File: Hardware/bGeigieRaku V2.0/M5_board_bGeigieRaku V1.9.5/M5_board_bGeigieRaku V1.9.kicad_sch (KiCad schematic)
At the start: 22 parts, among them J1 M5 2x15 pin, J10 QI GND, J11 QI charger Plus, J2 Geiger, J3 GPS, J4 Conn_01x14_Female, J5 Conn_01x14_Female, J6 Conn_01x14_Female, J7 Conn_01x14_Female, J8 QI charger GND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

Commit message: Updated board V1.9.6
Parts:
- removed J4, J5, J6: Conn_01x14_Female, Connector_PinHeader_2.54mm:PinHeader_1x18_P2.54mm_Vertical, symbol Connector:Conn_01x18_Female
- J1: footprint Connector_PinHeader_2.54mm:PinHeader_2x15_P2.54mm_Vertical -> Connector_PinHeader_2.54mm:PinHeader_2x15_P2.54mm_Vertical_SMD
- J3: footprint Connector_PinHeader_2.54mm:PinHeader_1x04_P2.54mm_Horizontal -> Connector_PinHeader_1.00mm:PinHeader_1x04_P1.00mm_Horizontal
- J7: symbol Connector:Conn_01x18_Female -> Connector:Conn_01x08_Male
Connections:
- net 3.3V: now also J2.1 (Pin_1); no longer J2.3 (Pin_3)
- net GND: now also J2.3 (Pin_3); no longer J2.1 (Pin_1)
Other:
- note added: "For SMD changes: 18650 footprint change J1 footprint change GPS footprint change"
- note added: "GPS Beitian Dual BN-220 GPS GLONASS Antenna Module TTL Level RC Drone Airplane"
- note added: "V1.9.6"
- note removed: "V1.9.5"

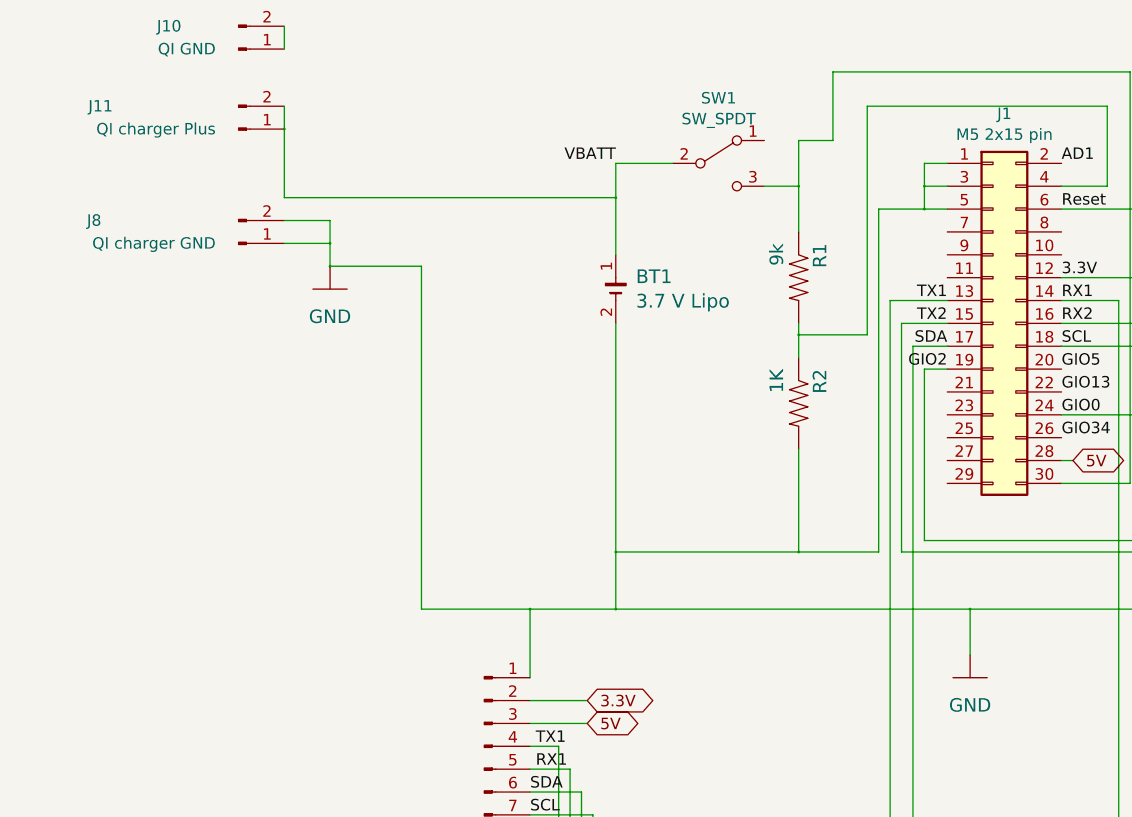
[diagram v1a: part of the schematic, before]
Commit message: added P channel MOSFET for protection.
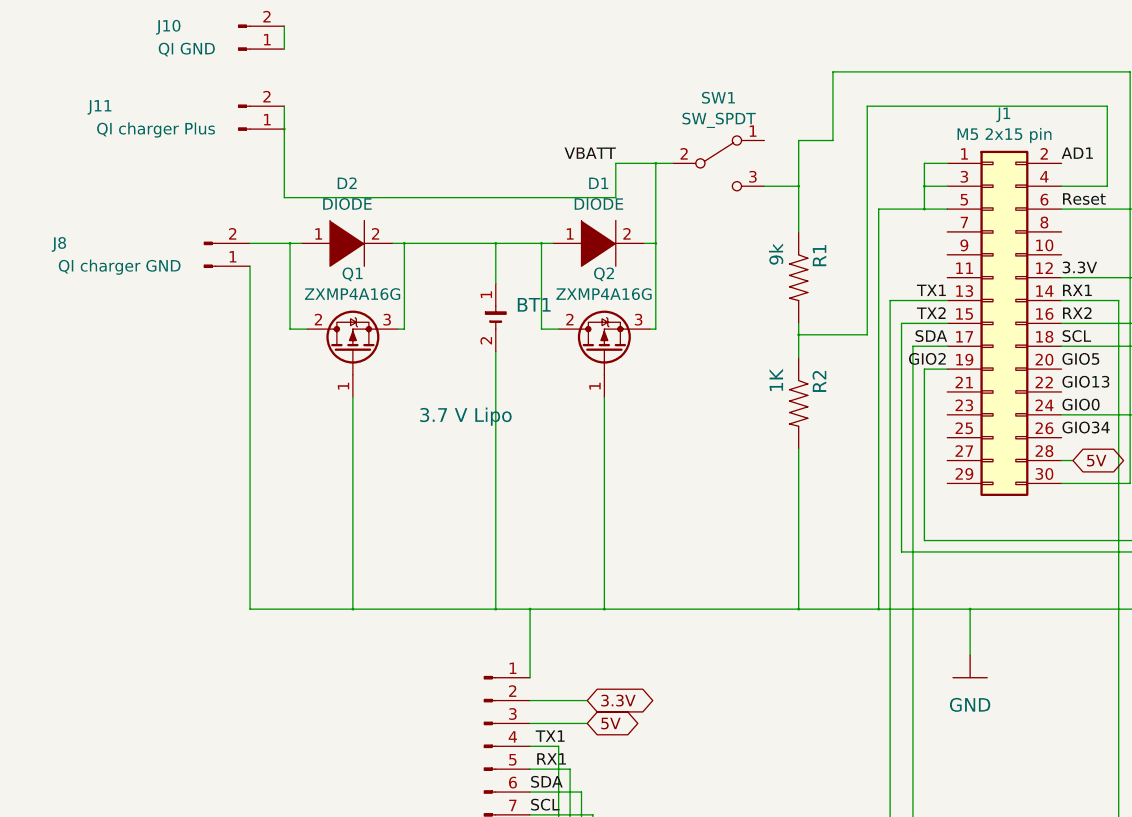
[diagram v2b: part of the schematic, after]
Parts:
- added D1, D2: DIODE, symbol pspice:DIODE
- added Q1, Q2: ZXMP4A16G, Package_TO_SOT_SMD:SOT-223-3_TabPin2, symbol Transistor_FET:ZXMP4A16G
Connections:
- net GND: now also Q1.1 (G), Q2.1 (G); no longer J8.2 (Pin_2)
- net VBATT: now also D1.2 (A), Q2.3 (S); no longer BT1.1 (+)
- new net: BT1.1 (+), D1.1 (K), D2.2 (A), Q1.3 (S), Q2.2 (D)
- new net: D2.1 (K), J8.2 (Pin_2), Q1.2 (D)
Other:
- moved on the sheet: BT1, J8

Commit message: added plates and small modifictaions
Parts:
- D1, D2: footprint (none) -> Diode_THT:D_DO-15_P15.24mm_Horizontal
- J3: footprint Connector_PinHeader_1.00mm:PinHeader_1x04_P1.00mm_Horizontal -> Connector_PinSocket_2.54mm:PinSocket_1x04_P2.54mm_Vertical
- J7: footprint Connector_PinHeader_2.54mm:PinHeader_1x18_P2.54mm_Vertical -> Connector_PinHeader_2.54mm:PinHeader_1x10_P2.54mm_Vertical
- Q1, Q2: value ZXMP4A16G -> IRF4905; footprint Package_TO_SOT_SMD:SOT-223-3_TabPin2 -> Package_TO_SOT_THT:TO-220-3_Vertical; symbol Transistor_FET:ZXMP4A16G -> Transistor_FET:IRF4905; Manf# (none) -> Digikey
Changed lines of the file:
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@@
   (symbol (lib_id "bGeigieRaku-V2-rescue:BATTERY-akizuki-M5_board-rescue") (at 83.185 93.345 0) (unit 1)
     (in_bom yes) (on_board yes)
-    (property "Reference" "BT1" (id 0) (at 85.4202 91.9734 0)
+    (property "Reference" "BT1" (id 0) (at 76.5302 101.4984 0)
       (effects (font (size 1.524 1.524)) (justify left))
     )
@@
       (effects (font (size 1.27 1.27)) (justify left))
     )
-    (property "Footprint" "Connector_PinHeader_1.00mm:PinHeader_1x04_P1.00mm_Horizontal" (id 2) (at 194.31 80.01 0)
+    (property "Footprint" "Connector_PinSocket_2.54mm:PinSocket_1x04_P2.54mm_Vertical" (id 2) (at 194.31 80.01 0)
       (effects (font (size 1.27 1.27)) hide)
     )
@@
     (property "Reference" "D2" (id 0) (at 66.675 78.4668 0))
     (property "Value" "DIODE" (id 1) (at 66.675 80.7655 0))
-    (property "Footprint" "" (id 2) (at 66.675 85.09 0)
+    (property "Footprint" "Diode_THT:D_DO-15_P15.24mm_Horizontal" (id 2) (at 66.675 85.09 0)
       (effects (font (size 1.27 1.27)) hide)
     )
@@
     (property "Reference" "D1" (id 0) (at 94.615 78.4668 0))
     (property "Value" "DIODE" (id 1) (at 94.615 80.7655 0))
-    (property "Footprint" "" (id 2) (at 94.615 85.09 0)
+    (property "Footprint" "Diode_THT:D_DO-15_P15.24mm_Horizontal" (id 2) (at 94.615 85.09 0)
       (effects (font (size 1.27 1.27)) hide)
     )
@@
       (effects (font (size 1.27 1.27)) (justify left) hide)
     )
-    (property "Footprint" "Connector_PinHeader_2.54mm:PinHeader_1x18_P2.54mm_Vertical" (id 2) (at 81.915 140.97 0)
+    (property "Footprint" "Connector_PinHeader_2.54mm:PinHeader_1x10_P2.54mm_Vertical" (id 2) (at 81.915 140.97 0)
       (effects (font (size 1.27 1.27)) hide)
     )
@@
     (pin "8")
   )
-  (symbol (lib_id "Transistor_FET:ZXMP4A16G") (at 67.31 97.155 90) (unit 1)
-    (in_bom yes) (on_board yes)
-    (property "Reference" "Q1" (id 0) (at 67.31 88.4744 90))
-    (property "Value" "ZXMP4A16G" (id 1) (at 67.31 90.7731 90))
-    (property "Footprint" "Package_TO_SOT_SMD:SOT-223-3_TabPin2" (id 2) (at 69.215 92.075 0)
+  (symbol (lib_id "Transistor_FET:IRF4905") (at 67.31 97.155 90) (unit 1)
+    (in_bom yes) (on_board yes)
+    (property "Reference" "Q1" (id 0) (at 66.04 100.33 90)
+      (effects (font (size 1.27 1.27)) (justify left))
+    )
+    (property "Value" "IRF4905" (id 1) (at 71.755 91.44 90)
+      (effects (font (size 1.27 1.27)) (justify left))
+    )
+    (property "Footprint" "Package_TO_SOT_THT:TO-220-3_Vertical" (id 2) (at 69.215 92.075 0)
       (effects (font (size 1.27 1.27) italic) (justify left) hide)
     )
-    (property "Datasheet" "https://www.diodes.com/assets/Datasheets/ZXMP4A16G.pdf" (id 3) (at 67.31 97.155 0)
-      (effects (font (size 1.27 1.27)) (justify left) hide)
-    )
-    (pin "1")
-    (pin "2")
-    (pin "3")
-  )
-  (symbol (lib_id "Transistor_FET:ZXMP4A16G") (at 95.25 97.155 90) (unit 1)
-    (in_bom yes) (on_board yes)
-    (property "Reference" "Q2" (id 0) (at 95.25 88.4744 90))
-    (property "Value" "ZXMP4A16G" (id 1) (at 95.25 90.7731 90))
-    (property "Footprint" "Package_TO_SOT_SMD:SOT-223-3_TabPin2" (id 2) (at 97.155 92.075 0)
+    (property "Datasheet" "https://www.digikey.com/en/products/detail/infineon-technologies/IRF4905LPBF/1928053" (id 3) (at 67.31 97.155 0)
+      (effects (font (size 1.27 1.27)) (justify left) hide)
+    )
+    (property "Manf#" "Digikey" (id 4) (at 67.31 97.155 0)
+      (effects (font (size 1.27 1.27)) hide)
+    )
+    (pin "1")
+    (pin "2")
+    (pin "3")
+  )
+  (symbol (lib_id "Transistor_FET:IRF4905") (at 95.25 97.155 90) (unit 1)
+    (in_bom yes) (on_board yes)
+    (property "Reference" "Q2" (id 0) (at 93.345 100.965 90)
+      (effects (font (size 1.27 1.27)) (justify left))
+    )
+    (property "Value" "IRF4905" (id 1) (at 99.06 91.44 90)
+      (effects (font (size 1.27 1.27)) (justify left))
+    )
+    (property "Footprint" "Package_TO_SOT_THT:TO-220-3_Vertical" (id 2) (at 97.155 92.075 0)
       (effects (font (size 1.27 1.27) italic) (justify left) hide)
     )
-    (property "Datasheet" "https://www.diodes.com/assets/Datasheets/ZXMP4A16G.pdf" (id 3) (at 95.25 97.155 0)
-      (effects (font (size 1.27 1.27)) (justify left) hide)
+    (property "Datasheet" "https://www.digikey.com/en/products/detail/infineon-technologies/IRF4905LPBF/1928053" (id 3) (at 95.25 97.155 0)
+      (effects (font (size 1.27 1.27)) (justify left) hide)
+    )
+    (property "Manf#" "Digikey" (id 4) (at 95.25 97.155 0)
+      (effects (font (size 1.27 1.27)) hide)
     )
     (pin "1")
@@
     )
     (path "/47993381-1a05-46c7-bbc4-e790f9bc1f17"
-      (reference "D1") (unit 1) (value "DIODE") (footprint "")
+      (reference "D1") (unit 1) (value "DIODE") (footprint "Diode_THT:D_DO-15_P15.24mm_Horizontal")
     )
     (path "/6bcf1216-48e4-4919-8192-c138cd0dd5e5"
-      (reference "D2") (unit 1) (value "DIODE") (footprint "")
+      (reference "D2") (unit 1) (value "DIODE") (footprint "Diode_THT:D_DO-15_P15.24mm_Horizontal")
     )
     (path "/fa951020-7499-42bc-bf77-1fbbed7d667f"
@@
     )
     (path "/00000000-0000-0000-0000-00005d536d8e"
-      (reference "J3") (unit 1) (value "GPS") (footprint "Connector_PinHeader_1.00mm:PinHeader_1x04_P1.00mm_Horizontal")
+      (reference "J3") (unit 1) (value "GPS") (footprint "Connector_PinSocket_2.54mm:PinSocket_1x04_P2.54mm_Vertical")
     )
     (path "/00000000-0000-0000-0000-00005da51168"
-      (reference "J7") (unit 1) (value "Conn_01x14_Female") (footprint "Connector_PinHeader_2.54mm:PinHeader_1x18_P2.54mm_Vertical")
+      (reference "J7") (unit 1) (value "Conn_01x14_Female") (footprint "Connector_PinHeader_2.54mm:PinHeader_1x10_P2.54mm_Vertical")
     )
     (path "/00000000-0000-0000-0000-00005da40adb"
@@
     )
     (path "/b749c318-7edd-4542-b93d-f083ca4c8e25"
-      (reference "Q1") (unit 1) (value "ZXMP4A16G") (footprint "Package_TO_SOT_SMD:SOT-223-3_TabPin2")
+      (reference "Q1") (unit 1) (value "IRF4905") (footprint "Package_TO_SOT_THT:TO-220-3_Vertical")
     )
     (path "/21d6682a-5eab-4a05-b431-39e8576a2c9d"
-      (reference "Q2") (unit 1) (value "ZXMP4A16G") (footprint "Package_TO_SOT_SMD:SOT-223-3_TabPin2")
+      (reference "Q2") (unit 1) (value "IRF4905") (footprint "Package_TO_SOT_THT:TO-220-3_Vertical")
     )
     (path "/00000000-0000-0000-0000-00005d6719f3"
